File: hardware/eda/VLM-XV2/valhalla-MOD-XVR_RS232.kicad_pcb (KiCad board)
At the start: 2 copper layers, 76.2 x 50.8 mm, 8 parts, among them J1 BUS, J2 RS232, J3 TTL, U1 ICL3232

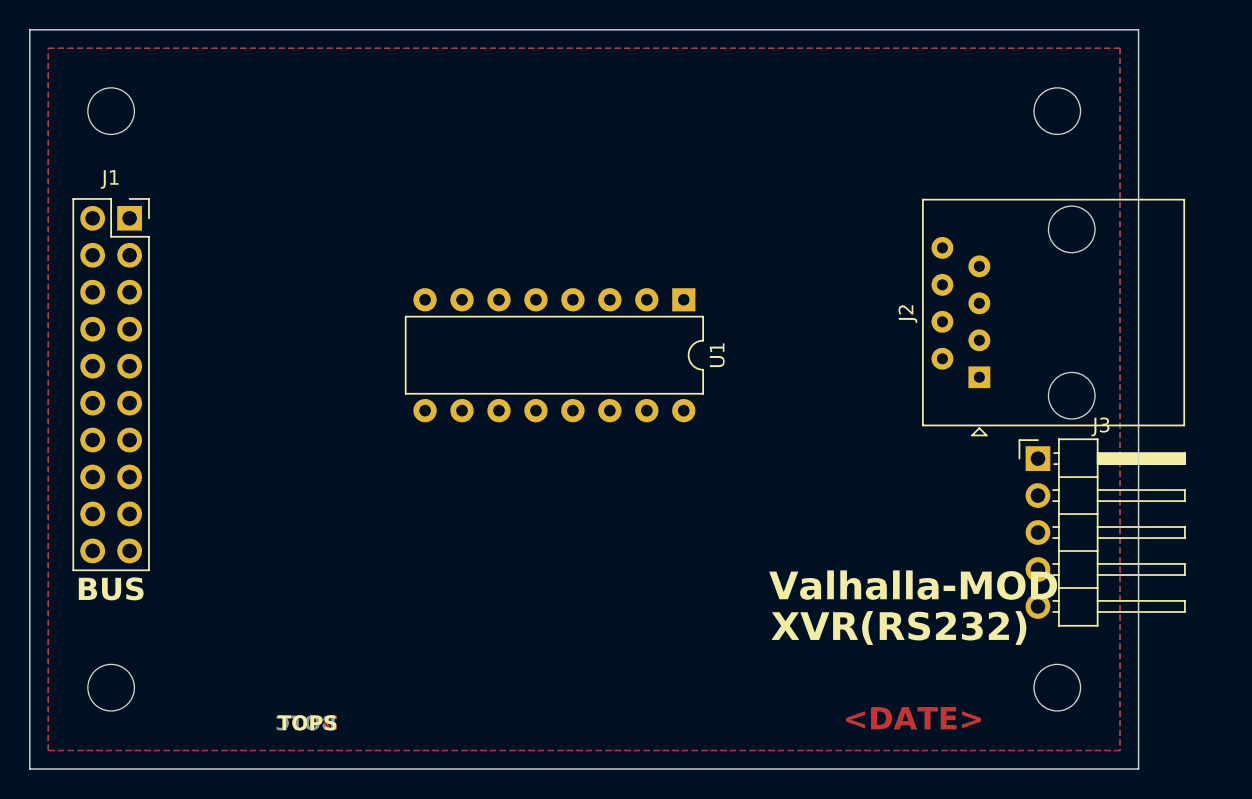
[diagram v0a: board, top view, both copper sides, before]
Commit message: UPDATE: core transceiver part done for XVR(RS232)
  - drawn and connected core components, placed on PCB tentatively
  - will probably go for the integrated 8P8C+LEDs jack to remain
    compliant with the Valhalla-MOD mechanical standard
  - some assembly time configurability avenues identified, next to
    implement.
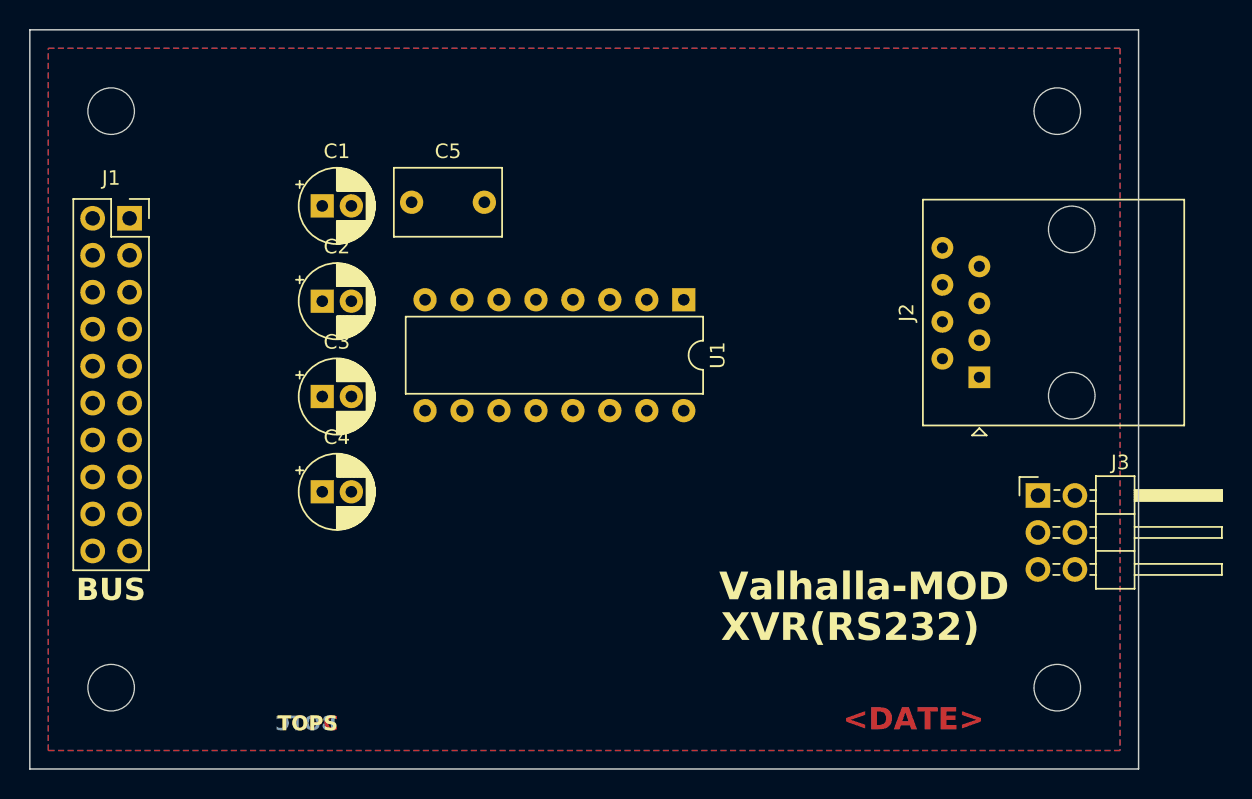
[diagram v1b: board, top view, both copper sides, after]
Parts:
- added C1: 1uF, Capacitor_THT:CP_Radial_D5.0mm_P2.00mm, F.Cu at (88.7, 47.7)
- added C2: 1uF, Capacitor_THT:CP_Radial_D5.0mm_P2.00mm, F.Cu at (88.7, 54.2)
- added C3: 1uF, Capacitor_THT:CP_Radial_D5.0mm_P2.00mm, F.Cu at (88.7, 60.8)
- added C4: 1uF, Capacitor_THT:CP_Radial_D5.0mm_P2.00mm, F.Cu at (88.7, 67.3)
- added C5: 0.1uF, Capacitor_THT:C_Rect_L7.2mm_W4.5mm_P5.00mm_FKS2_FKP2_MKS2_MKP2, F.Cu at (94.8, 47.4)
- J3: footprint Connector_PinHeader_2.54mm:PinHeader_1x05_P2.54mm_Horizontal -> Connector_PinHeader_2.54mm:PinHeader_2x03_P2.54mm_Horizontal
- moved J3 2.53 mm to (137.9, 67.6)
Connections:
- J1 pad 1: /AVCC -> unconnected-(J1-Pin_1-Pad1)
- J1 pad 10: /~{SS} -> unconnected-(J1-Pin_10-Pad10)
- J1 pad 11: /~{SINT} -> unconnected-(J1-Pin_11-Pad11)
- J1 pad 13: /SDA -> unconnected-(J1-Pin_13-Pad13)
- J1 pad 14: /SCL -> unconnected-(J1-Pin_14-Pad14)
- J1 pad 15: /~{IINT} -> unconnected-(J1-Pin_15-Pad15)
- J1 pad 2: /AGND -> unconnected-(J1-Pin_2-Pad2)
- J1 pad 7: /MOSI -> unconnected-(J1-Pin_7-Pad7)
- J1 pad 8: /MISO -> unconnected-(J1-Pin_8-Pad8)
- J1 pad 9: /SCK -> unconnected-(J1-Pin_9-Pad9)
- U1 pad 1: unconnected-(U1-C1+-Pad1) -> Net-(U1-C1+)
- U1 pad 2: unconnected-(U1-VS+-Pad2) -> Net-(U1-VS+)
- U1 pad 3: unconnected-(U1-C1--Pad3) -> Net-(U1-C1-)
- U1 pad 4: unconnected-(U1-C2+-Pad4) -> Net-(U1-C2+)
- U1 pad 5: unconnected-(U1-C2--Pad5) -> Net-(U1-C2-)
- U1 pad 6: unconnected-(U1-VS--Pad6) -> Net-(U1-VS-)

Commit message: UPDATE: Schematic done for XVR(RS-232)
  - gave up on native modularity in KiCAD, the data model is simply
    broken
  - routing of XVR(RS-232) to commence next.
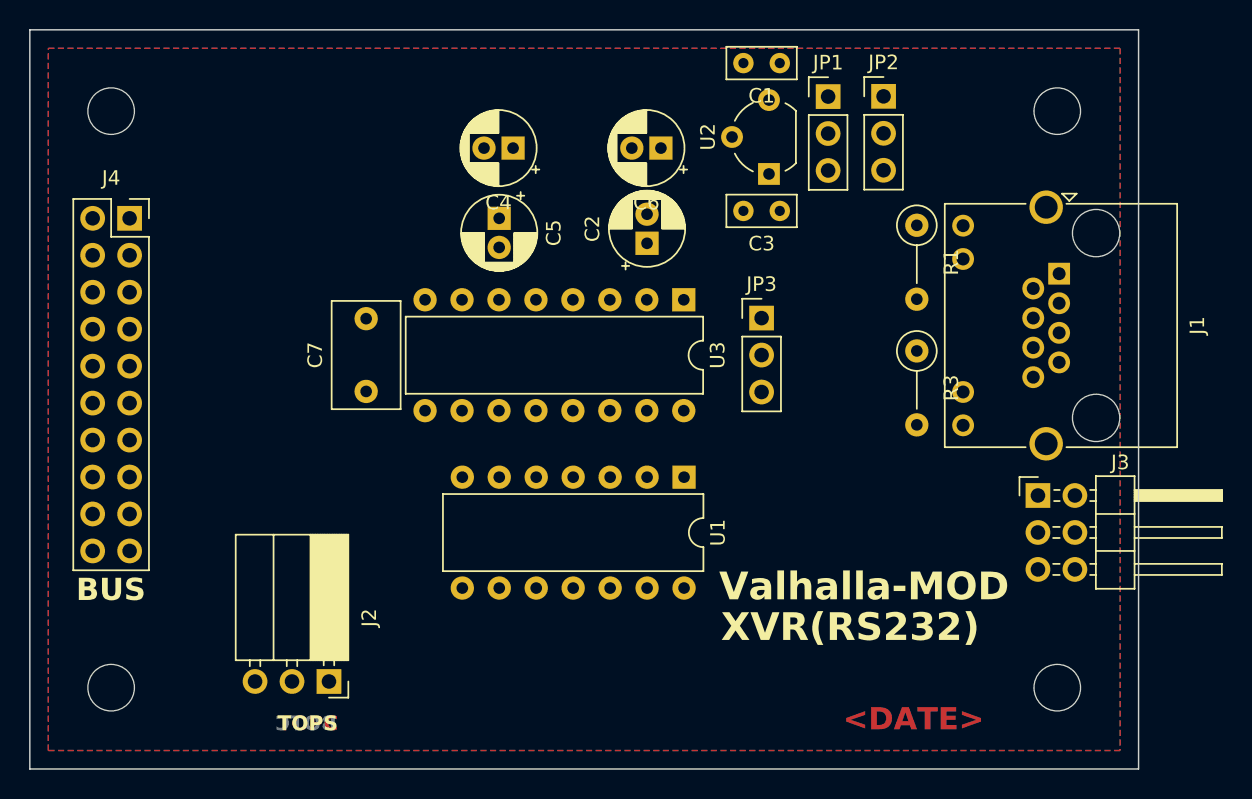
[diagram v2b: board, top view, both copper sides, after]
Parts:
- added C1: 330nF, Capacitor_THT:C_Rect_L4.6mm_W2.0mm_P2.50mm_MKS02_FKP02, F.Cu at (120.1, 37.8)
- added C3: 0.1uF, Capacitor_THT:C_Rect_L4.6mm_W2.0mm_P2.50mm_MKS02_FKP02, F.Cu at (120.1, 48.0)
- added J1: RS-232, Connector_RJ:RJ45_Amphenol_RJHSE538X, F.Cu at (139.3, 52.3)
- added JP1: LED_VCC3, Connector_PinHeader_2.54mm:PinHeader_1x03_P2.54mm_Vertical, F.Cu at (123.4, 40.1)
- added JP2: LED_VCC5, Connector_PinHeader_2.54mm:PinHeader_1x03_P2.54mm_Vertical, F.Cu at (127.3, 40.1)
- added JP3: XVR_VCC, Connector_PinHeader_2.54mm:PinHeader_1x03_P2.54mm_Vertical, F.Cu at (118.9, 55.4)
- added R1: *1, Resistor_THT:R_Axial_DIN0207_L6.3mm_D2.5mm_P5.08mm_Vertical, F.Cu at (129.5, 49.0)
- added R3: *1, Resistor_THT:R_Axial_DIN0207_L6.3mm_D2.5mm_P5.08mm_Vertical, F.Cu at (129.5, 57.6)
- added U1: 74LS06, Package_DIP:DIP-14_W7.62mm, F.Cu at (113.5, 66.3)
- added U2: L78L33_TO92, Package_TO_SOT_THT:TO-92_Wide, F.Cu at (119.4, 45.5)
- J2: value RS232 -> POLOLU-4941; footprint Connector_RJ:RJ45_Amphenol_54602-x08_Horizontal -> Connector_PinSocket_2.54mm:PinSocket_1x03_P2.54mm_Horizontal
- moved J2 49.3 mm to (89.1, 80.3), turned to -90 degrees
- moved C2 24.7 mm to (111.0, 50.2), turned to 90 degrees
- moved C6 23.6 mm to (112.0, 43.7), turned to 180 degrees
- moved C5 22.4 mm to (100.8, 48.5), turned to -90 degrees
- moved C4 16.8 mm to (101.8, 43.7), turned to 180 degrees
- moved C7 13.4 mm to (91.7, 60.4), turned to 90 degrees
- renumbered C3 to C2, C2 to C4, C4 to C5, C1 to C6, C5 to C7, J1 to J4, U1 to U3
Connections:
- C7 pad 1: /DVCC -> Net-(JP3-C)
- J2 pad 1: Net-(U1-T2OUT) -> /DVCC
- J2 pad 2: unconnected-(J2-Pad2) -> /DGND
- J2 pad 3: Net-(U1-T1OUT) -> Net-(J2-Pin_3)
- U3 pad 13: Net-(U1-R1IN) -> Net-(U3-R1IN)
- U3 pad 14: Net-(U1-T1OUT) -> Net-(U3-T1OUT)
- U3 pad 16: /DVCC -> Net-(JP3-C)
- U3 pad 7: Net-(U1-T2OUT) -> Net-(U3-T2OUT)
- U3 pad 8: Net-(U1-R2IN) -> Net-(U3-R2IN)

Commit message: UPDATE: XVR(RS-232) done, RTM
  - layout and routing done for XVR(RS-232), including documentation
    for assembly variants and volumetric interference checks.
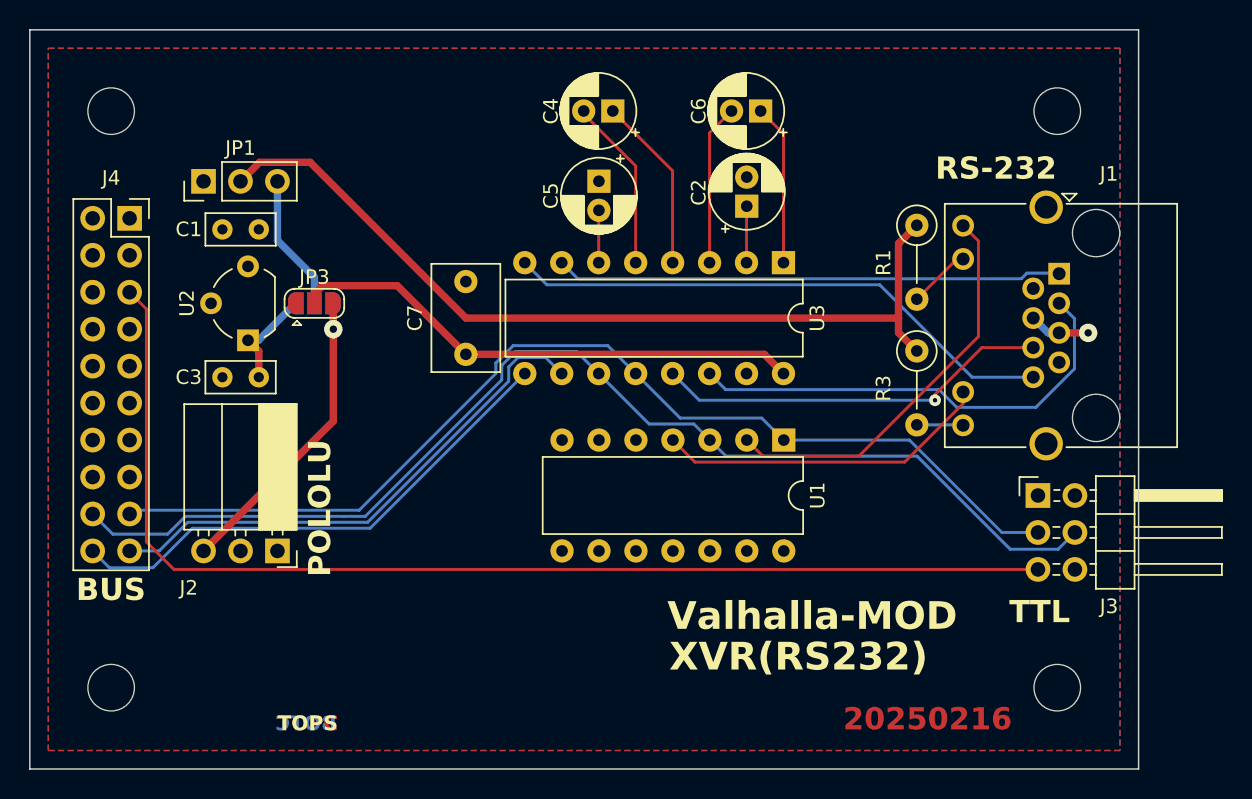
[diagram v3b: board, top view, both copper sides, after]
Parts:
- JP2: footprint Connector_PinHeader_2.54mm:PinHeader_1x03_P2.54mm_Vertical -> Jumper:SolderJumper-3_P1.3mm_Open_RoundedPad1.0x1.5mm; moved to B.Cu
- JP3: footprint Connector_PinHeader_2.54mm:PinHeader_1x03_P2.54mm_Vertical -> Jumper:SolderJumper-3_P1.3mm_Open_RoundedPad1.0x1.5mm
- U3: value ICL3232 -> *2
- moved JP1 43.3 mm to (80.5, 46.0), turned to 90 degrees
- moved JP2 41.6 mm to (88.1, 54.4)
- moved C1 37.6 mm to (84.3, 49.3)
- moved C3 37.6 mm to (84.3, 59.4)
- moved U2 37.6 mm to (83.6, 56.9)
- moved JP3 30.8 mm to (88.1, 54.4)
- moved J2 9.65 mm to (85.6, 71.4)
- moved C5 7.31 mm to (107.7, 46.0)
- moved U3 7.31 mm to (120.4, 51.6)
- moved C4 7.31 mm to (108.6, 41.1)
- moved C6 7.31 mm to (118.8, 41.1)
- moved U1 7.31 mm to (120.4, 63.8)
- moved C2 7.31 mm to (117.9, 47.7)
- moved C7 7.31 mm to (98.5, 57.9)
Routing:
- net /TXDO: track 0.00 -> 80.0 mm
- net /~{RESET}: track 0.00 -> 79.7 mm
- net /RXDI: track 0.00 -> 73.0 mm
- net /LVCC: track 0.00 -> 59.9 mm
- net Net-(U3-R2IN): track 0.00 -> 38.2 mm
- net /~{RTS}: track 0.00 -> 36.2 mm
- net /~{DCD}: track 0.00 -> 35.7 mm
- net Net-(JP3-C): track 0.00 -> 35.6 mm
- net Net-(U3-T2OUT): track 0.00 -> 34.8 mm
- net Net-(U3-T1OUT): track 0.00 -> 32.1 mm
- net Net-(J1-Pad9): track 0.00 -> 27.8 mm
- net Net-(U3-R1IN): track 0.00 -> 27.3 mm, vias 0 -> 1
- net Net-(J1-Pad11): track 0.00 -> 23.0 mm
- net Net-(J2-Pin_3): track 0.00 -> 22.5 mm, vias 0 -> 1
- net Net-(U3-C2+): track 0.00 -> 12.1 mm
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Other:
- board text added: "20250216"
- board text added: "POLOLU"
- board text added: "RS-232"
- board text added: "TTL"
- board text removed: "<DATE>"

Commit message: UPDATE: updated MOD-XVR(RS232) to match the latest specification.
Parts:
- removed C1: 330nF, Capacitor_THT:C_Rect_L4.6mm_W2.0mm_P2.50mm_MKS02_FKP02
- removed C3: 0.1uF, Capacitor_THT:C_Rect_L4.6mm_W2.0mm_P2.50mm_MKS02_FKP02
- removed J2: POLOLU-4941, Connector_PinSocket_2.54mm:PinSocket_1x03_P2.54mm_Horizontal
- removed JP1: LED_VCC3, Connector_PinHeader_2.54mm:PinHeader_1x03_P2.54mm_Vertical
- removed JP2: LED_VCC5, Jumper:SolderJumper-3_P1.3mm_Open_RoundedPad1.0x1.5mm
- removed JP3: XVR_VCC, Jumper:SolderJumper-3_P1.3mm_Open_RoundedPad1.0x1.5mm
- removed U2: L78L33_TO92, Package_TO_SOT_THT:TO-92_Wide
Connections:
- C7 pad 1: Net-(JP3-C) -> /DVCC
- J4 pad 16: unconnected-(J4-Pin_16-Pad16) -> /LVCC
- J4 pad 6: unconnected-(J4-Pin_6-Pad6) -> /DGND
- U3 pad 16: Net-(JP3-C) -> /DVCC
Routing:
- net Net-(JP3-C): track 35.6 -> 0.00 mm
- net Net-(J2-Pin_3): track 22.5 -> 0.00 mm, vias 1 -> 0
- net /LVCC: track 59.9 -> 80.3 mm
- net Net-(JP1-B): track 9.43 -> 0.00 mm
- net Net-(JP2-A): track 7.16 -> 0.00 mm
- net /~{RESET}: track 79.7 -> 73.0 mm, vias 0 -> 2
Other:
- board text added: "20250325"
- board text removed: "20250216"
- board text removed: "POLOLU"
